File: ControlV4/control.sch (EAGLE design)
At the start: 45 parts, among them P1 CONNEC_1X03, P10 CONNEC_1X03, P11 CONNEC_1X03, P12 CONNEC_1X03, P2 CONNEC_1X03, P3 CONNEC_1X03, P4 CONNEC_1X03, P5 CONNEC_1X03, P6 CONNEC_1X03, P7 CONNEC_1X03, P8 CONNEC_1X03, P9 CONNEC_1X03

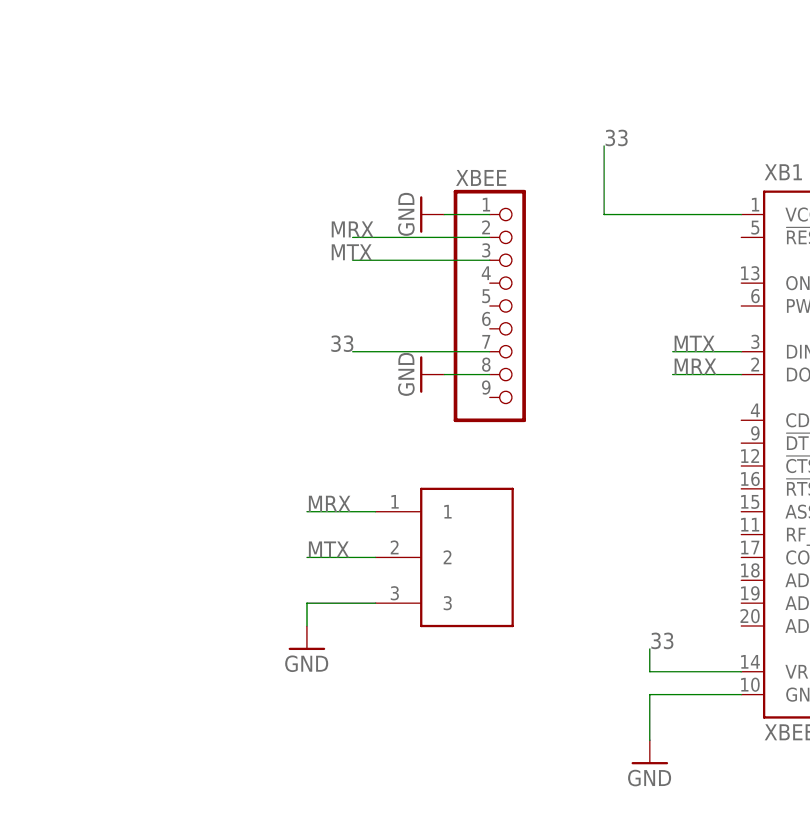
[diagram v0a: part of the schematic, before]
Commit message: Removing unused XBee port, changing extra serial port to 2.54
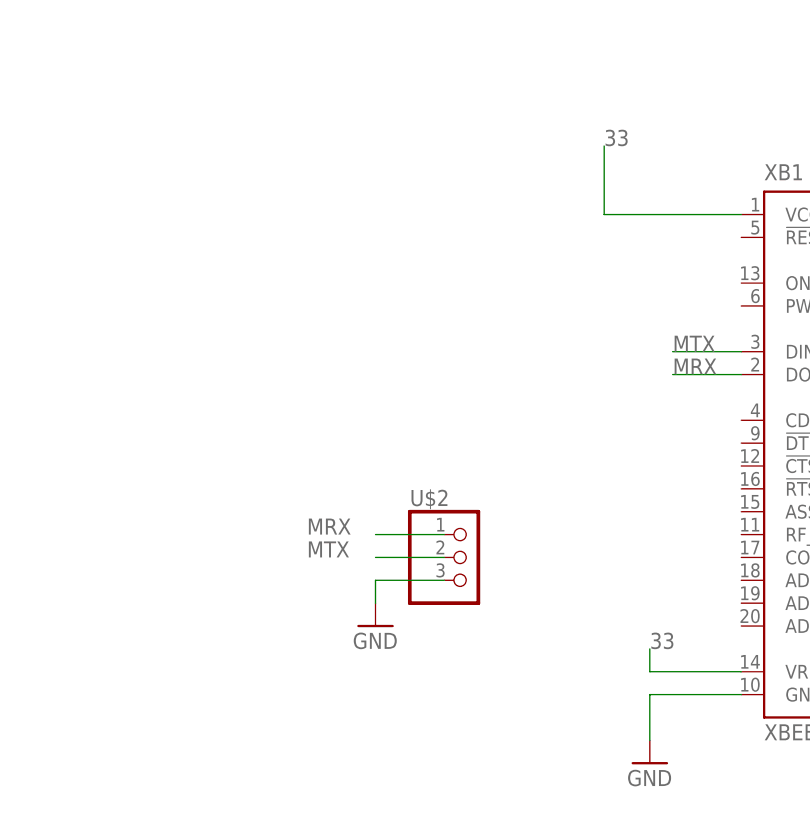
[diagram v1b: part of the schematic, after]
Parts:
- removed U$9: JST_3, perso:JST_3
- removed XBEE: CONNEC_1X09, rhoban:CONNEC_1X09
- added U$2: CONNEC_1X03, RobotCampus:CONNEC_1X03
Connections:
- net 33: no longer XBEE.7
- net GND: now also U$2.3; no longer U$9.3, XBEE.1, XBEE.8
- net MRX: now also U$2.1; no longer U$9.1, XBEE.2
- net MTX: now also U$2.2; no longer U$9.2, XBEE.3
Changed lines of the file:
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@@
 <part name="R11" library="rhoban" deviceset="RESISTANCE" device="-R0805"/>
 <part name="R12" library="rhoban" deviceset="RESISTANCE" device="-R0805"/>
-<part name="XBEE" library="rhoban" deviceset="CONNEC_1X09" device=""/>
-<part name="GND13" library="supply1" deviceset="GND" device=""/>
-<part name="GND14" library="supply1" deviceset="GND" device=""/>
 <part name="C1" library="rcl" deviceset="C-EU" device="075-032X103"/>
 <part name="C2" library="rcl" deviceset="C-EU" device="075-032X103"/>
@@
 <part name="GND15" library="supply1" deviceset="GND" device=""/>
 <part name="U$8" library="perso" deviceset="JST_2" device=""/>
-<part name="U$9" library="perso" deviceset="JST_3" device=""/>
 <part name="U$10" library="perso" deviceset="JST_2" device=""/>
 <part name="R13" library="rcl" deviceset="R-EU_" device="R0805"/>
@@
 <part name="U$12" library="RobotCampus" deviceset="DIODE" device=""/>
 <part name="JP1" library="pinhead" deviceset="PINHD-1X3" device=""/>
+<part name="U$2" library="RobotCampus" deviceset="CONNEC_1X03" device=""/>
 </parts>
 <sheets>
@@
 <instance part="P+2" gate="VCC" x="248.92" y="116.84"/>
 <instance part="GND3" gate="1" x="251.46" y="60.96"/>
-<instance part="GND4" gate="1" x="91.44" y="-22.86"/>
+<instance part="GND4" gate="1" x="99.06" y="-20.32"/>
 <instance part="GND5" gate="1" x="58.42" y="144.78"/>
 <instance part="P+3" gate="VCC" x="58.42" y="160.02"/>
@@
 <instance part="R11" gate="G$1" x="236.22" y="99.06"/>
 <instance part="R12" gate="G$1" x="236.22" y="106.68"/>
-<instance part="XBEE" gate="G$1" x="109.22" y="15.24"/>
-<instance part="GND13" gate="1" x="104.14" y="25.4" rot="R270"/>
-<instance part="GND14" gate="1" x="104.14" y="7.62" rot="R270"/>
 <instance part="C1" gate="G$1" x="210.82" y="152.4"/>
 <instance part="C2" gate="G$1" x="218.44" y="152.4"/>
@@
 <instance part="GND15" gate="1" x="58.42" y="127"/>
 <instance part="U$8" gate="G$1" x="73.66" y="132.08"/>
-<instance part="U$9" gate="G$1" x="109.22" y="-12.7"/>
 <instance part="U$10" gate="G$1" x="73.66" y="152.4"/>
 <instance part="R13" gate="G$1" x="45.72" y="91.44"/>
@@
 <instance part="U$12" gate="DIODE" x="157.48" y="172.72"/>
 <instance part="JP1" gate="A" x="187.96" y="170.18" rot="MR180"/>
+<instance part="U$2" gate="G$1" x="104.14" y="-15.24"/>
 </instances>
 <busses>
@@
 </segment>
 <segment>
-<pinref part="XBEE" gate="G$1" pin="1"/>
-<pinref part="GND13" gate="1" pin="GND"/>
-<wire x1="106.68" y1="25.4" x2="111.76" y2="25.4" width="0.1524" layer="91"/>
-</segment>
-<segment>
-<pinref part="XBEE" gate="G$1" pin="8"/>
-<pinref part="GND14" gate="1" pin="GND"/>
-<wire x1="106.68" y1="7.62" x2="111.76" y2="7.62" width="0.1524" layer="91"/>
-</segment>
-<segment>
 <pinref part="GND15" gate="1" pin="GND"/>
 <pinref part="U$8" gate="G$1" pin="GND"/>
 <wire x1="58.42" y1="129.54" x2="63.5" y2="129.54" width="0.1524" layer="91"/>
-</segment>
-<segment>
-<pinref part="U$9" gate="G$1" pin="3"/>
-<wire x1="99.06" y1="-17.78" x2="91.44" y2="-17.78" width="0.1524" layer="91"/>
-<wire x1="91.44" y1="-17.78" x2="91.44" y2="-20.32" width="0.1524" layer="91"/>
-<pinref part="GND4" gate="1" pin="GND"/>
 </segment>
 <segment>
@@
 <wire x1="129.54" y1="-27.94" x2="129.54" y2="-33.02" width="0.1524" layer="91"/>
 <pinref part="GND16" gate="1" pin="GND"/>
+</segment>
+<segment>
+<pinref part="U$2" gate="G$1" pin="3"/>
+<wire x1="106.68" y1="-15.24" x2="99.06" y2="-15.24" width="0.1524" layer="91"/>
+<pinref part="GND4" gate="1" pin="GND"/>
+<wire x1="99.06" y1="-15.24" x2="99.06" y2="-17.78" width="0.1524" layer="91"/>
 </segment>
 </net>
@@
 </segment>
 <segment>
-<pinref part="XBEE" gate="G$1" pin="3"/>
-<wire x1="111.76" y1="20.32" x2="96.52" y2="20.32" width="0.1524" layer="91"/>
-<label x="93.98" y="20.32" size="1.778" layer="95"/>
-</segment>
-<segment>
-<pinref part="U$9" gate="G$1" pin="2"/>
-<wire x1="99.06" y1="-12.7" x2="91.44" y2="-12.7" width="0.1524" layer="91"/>
-<label x="91.44" y="-12.7" size="1.778" layer="95"/>
-</segment>
-<segment>
 <pinref part="XB1" gate="G$1" pin="DIN/!CONFIG"/>
 <wire x1="139.7" y1="10.16" x2="132.08" y2="10.16" width="0.1524" layer="91"/>
 <label x="132.08" y="10.16" size="1.778" layer="95"/>
 </segment>
+<segment>
+<pinref part="U$2" gate="G$1" pin="2"/>
+<wire x1="106.68" y1="-12.7" x2="99.06" y2="-12.7" width="0.1524" layer="91"/>
+<label x="91.44" y="-12.7" size="1.778" layer="95"/>
+</segment>
 </net>
 <net name="MRX" class="0">
@@
 </segment>
 <segment>
-<pinref part="XBEE" gate="G$1" pin="2"/>
-<wire x1="111.76" y1="22.86" x2="96.52" y2="22.86" width="0.1524" layer="91"/>
-<label x="93.98" y="22.86" size="1.778" layer="95"/>
-</segment>
-<segment>
-<pinref part="U$9" gate="G$1" pin="1"/>
-<wire x1="99.06" y1="-7.62" x2="91.44" y2="-7.62" width="0.1524" layer="91"/>
-<label x="91.44" y="-7.62" size="1.778" layer="95"/>
-</segment>
-<segment>
 <pinref part="XB1" gate="G$1" pin="DOUT"/>
 <wire x1="139.7" y1="7.62" x2="132.08" y2="7.62" width="0.1524" layer="91"/>
 <label x="132.08" y="7.62" size="1.778" layer="95"/>
+</segment>
+<segment>
+<pinref part="U$2" gate="G$1" pin="1"/>
+<wire x1="106.68" y1="-10.16" x2="99.06" y2="-10.16" width="0.1524" layer="91"/>
+<label x="91.44" y="-10.16" size="1.778" layer="95"/>
 </segment>
 </net>
@@
 </segment>
 <segment>
-<pinref part="XBEE" gate="G$1" pin="7"/>
-<wire x1="111.76" y1="10.16" x2="96.52" y2="10.16" width="0.1524" layer="91"/>
-<label x="93.98" y="10.16" size="1.778" layer="95"/>
-</segment>
-<segment>

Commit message: Fixs
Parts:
- added C5: (no value), SparkFun-Capacitors:CAP_POLPTH2
- added R15, R16: (no value), rcl:R-EU_R0805
- added U$3: DIODE254, RobotCampus:DIODE254
- C3, C4: device rcl:C-EU075-032X103 -> SparkFun-Capacitors:CAP_POLPTH2
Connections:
- removed net MAPLE_VCC: C1.1, C2.1, JP1.2, R13.1, U$1.VIN, U$11.VIN
- removed net VCC: C3.1, C4.1, P1.2, P10.2, P11.2, P12.2, P2.2, P3.2, P4.2, P5.2, P6.2, P7.2, P8.2, P9.2, U$10.VCC
- new net N$13: R15.2, XB1.!RESET
- new net N$15: R16.2, XB1.ON/!SLEEP
- new net VMICRO: C3.+, C5.+, U$1.VIN, U$10.VCC, U$11.VIN, U$3.C
- new net VPOWER: C1.1, C2.1, C4.+, JP1.2, P1.2, P10.2, P11.2, P12.2, P2.2, P3.2, P4.2, P5.2, P6.2, P7.2, P8.2, P9.2, U$3.A
- net 33: now also R15.1, R16.1
- net GND: now also C3.-, C4.-, C5.-; no longer C3.2, C4.2
- net VCC_IN: now also R13.1

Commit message: Boarding
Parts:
- removed U$11: MCP1703SOT23-A, RobotCampus:MCP1703SOT23-A
- added C6: (no value), SparkFun-Capacitors:CAP_POLPTH2
- added U$4: MCP1703T-3302E/CB, RobotCampus:MCP1703T-3302E/CB
- renumbered U$10 to JST_MICRO, U$8 to JST_IN
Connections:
- new net 3.3: C6.+, U$4.VOUT
- net 33: no longer U$11.VOUT
- net GND: now also C6.-, U$4.GND; no longer U$11.GND
- net VMICRO: now also U$4.VIN; no longer U$11.VIN
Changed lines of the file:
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@@
 <part name="GPIO4" library="rhoban" deviceset="CONNEC_1X02" device=""/>
 <part name="GND6" library="supply1" deviceset="GND" device=""/>
-<part name="GND7" library="supply1" deviceset="GND" device=""/>
 <part name="GND8" library="supply1" deviceset="GND" device=""/>
 <part name="GND9" library="supply1" deviceset="GND" device=""/>
@@
 <part name="C2" library="rcl" deviceset="C-EU" device="075-032X103"/>
 <part name="GND15" library="supply1" deviceset="GND" device=""/>
-<part name="U$8" library="perso" deviceset="JST_2" device=""/>
-<part name="U$10" library="perso" deviceset="JST_2" device=""/>
+<part name="JST_IN" library="perso" deviceset="JST_2" device=""/>
+<part name="JST_MICRO" library="perso" deviceset="JST_2" device=""/>
 <part name="R13" library="rcl" deviceset="R-EU_" device="R0805"/>
 <part name="R14" library="rcl" deviceset="R-EU_" device="R0805"/>
@@
 <part name="XB1" library="maxstream" deviceset="XBEE" device="-PRO"/>
 <part name="GND16" library="supply1" deviceset="GND" device=""/>
-<part name="U$11" library="RobotCampus" deviceset="MCP1703" device="SOT23-A"/>
 <part name="U$12" library="RobotCampus" deviceset="DIODE" device=""/>
 <part name="JP1" library="pinhead" deviceset="PINHD-1X3" device=""/>
@@
 <part name="R15" library="rcl" deviceset="R-EU_" device="R0805"/>
 <part name="R16" library="rcl" deviceset="R-EU_" device="R0805"/>
+<part name="C6" library="SparkFun-Capacitors" deviceset="CAP_POL" device="PTH2"/>
+<part name="GND14" library="supply1" deviceset="GND" device=""/>
+<part name="U$4" library="RobotCampus" deviceset="MCP1703T-3302E/CB" device=""/>
+<part name="GND7" library="supply1" deviceset="GND" device=""/>
 </parts>
 <sheets>
@@
 <instance part="GPIO4" gate="G$1" x="251.46" y="-7.62" rot="R90"/>
 <instance part="GND6" gate="1" x="251.46" y="-12.7"/>
-<instance part="GND7" gate="1" x="160.02" y="119.38"/>
 <instance part="GND8" gate="1" x="218.44" y="142.24"/>
 <instance part="GND9" gate="1" x="210.82" y="142.24"/>
@@
 <instance part="C2" gate="G$1" x="218.44" y="152.4"/>
 <instance part="GND15" gate="1" x="58.42" y="127"/>
-<instance part="U$8" gate="G$1" x="73.66" y="132.08"/>
-<instance part="U$10" gate="G$1" x="73.66" y="152.4"/>
+<instance part="JST_IN" gate="G$1" x="73.66" y="132.08"/>
+<instance part="JST_MICRO" gate="G$1" x="73.66" y="152.4"/>
 <instance part="R13" gate="G$1" x="45.72" y="91.44"/>
 <instance part="R14" gate="G$1" x="53.34" y="86.36" rot="R90"/>
@@
 <instance part="XB1" gate="G$1" x="154.94" y="0"/>
 <instance part="GND16" gate="1" x="129.54" y="-35.56"/>
-<instance part="U$11" gate="G$1" x="160.02" y="152.4"/>
 <instance part="U$12" gate="DIODE" x="157.48" y="172.72"/>
 <instance part="JP1" gate="A" x="187.96" y="170.18" rot="MR180"/>
@@
 <instance part="R15" gate="G$1" x="134.62" y="22.86"/>
 <instance part="R16" gate="G$1" x="134.62" y="17.78"/>
+<instance part="C6" gate="G$1" x="276.86" y="152.4"/>
+<instance part="GND14" gate="1" x="276.86" y="142.24"/>
+<instance part="U$4" gate="A" x="149.86" y="149.86"/>
+<instance part="GND7" gate="1" x="129.54" y="139.7"/>
 </instances>
 <busses>
@@
 <pinref part="GND5" gate="1" pin="GND"/>
 <wire x1="58.42" y1="149.86" x2="58.42" y2="147.32" width="0.1524" layer="91"/>
-<pinref part="U$10" gate="G$1" pin="GND"/>
+<pinref part="JST_MICRO" gate="G$1" pin="GND"/>
 </segment>
 <segment>
@@
 </segment>
 <segment>
-<pinref part="GND7" gate="1" pin="GND"/>
-<wire x1="160.02" y1="121.92" x2="160.02" y2="142.24" width="0.1524" layer="91"/>
-<pinref part="U$11" gate="G$1" pin="GND"/>
-</segment>
-<segment>
 <pinref part="GND8" gate="1" pin="GND"/>
 <wire x1="218.44" y1="144.78" x2="218.44" y2="147.32" width="0.1524" layer="91"/>
@@
 <segment>
 <pinref part="GND15" gate="1" pin="GND"/>
-<pinref part="U$8" gate="G$1" pin="GND"/>
+<pinref part="JST_IN" gate="G$1" pin="GND"/>
 <wire x1="58.42" y1="129.54" x2="63.5" y2="129.54" width="0.1524" layer="91"/>
 </segment>
@@
 <pinref part="GND13" gate="1" pin="GND"/>
 <pinref part="C4" gate="G$1" pin="-"/>
+</segment>
+<segment>
+<pinref part="GND14" gate="1" pin="GND"/>
+<pinref part="C6" gate="G$1" pin="-"/>
+<wire x1="276.86" y1="144.78" x2="276.86" y2="147.32" width="0.1524" layer="91"/>
+</segment>
+<segment>
+<pinref part="U$4" gate="A" pin="GND"/>
+<pinref part="GND7" gate="1" pin="GND"/>
+<wire x1="132.08" y1="144.78" x2="129.54" y2="144.78" width="0.1524" layer="91"/>
+<wire x1="129.54" y1="144.78" x2="129.54" y2="142.24" width="0.1524" layer="91"/>
 </segment>
 </net>
@@
 </segment>
 </net>
-<net name="VPOWER" class="0">
+<net name="VPOWER" class="1">
 <segment>
 <wire x1="218.44" y1="154.94" x2="210.82" y2="154.94" width="0.1524" layer="91"/>
@@
 <net name="33" class="0">
 <segment>
-<wire x1="172.72" y1="154.94" x2="180.34" y2="154.94" width="0.1524" layer="91"/>
-<label x="180.34" y="154.94" size="1.778" layer="95"/>
-<pinref part="U$11" gate="G$1" pin="VOUT"/>
-</segment>
-<segment>
 <pinref part="XB1" gate="G$1" pin="VCC"/>
 <wire x1="139.7" y1="25.4" x2="124.46" y2="25.4" width="0.1524" layer="91"/>
@@
 <net name="VCC_IN" class="0">
 <segment>
-<pinref part="U$8" gate="G$1" pin="VCC"/>
+<pinref part="JST_IN" gate="G$1" pin="VCC"/>
 <wire x1="63.5" y1="134.62" x2="58.42" y2="134.62" width="0.1524" layer="91"/>
 <label x="50.8" y="134.62" size="1.778" layer="95"/>
@@
 <segment>
 <wire x1="63.5" y1="154.94" x2="58.42" y2="154.94" width="0.1524" layer="91"/>
-<pinref part="U$10" gate="G$1" pin="VCC"/>
+<pinref part="JST_MICRO" gate="G$1" pin="VCC"/>
 <label x="58.42" y="157.48" size="1.778" layer="95" rot="R180"/>
 </segment>
@@
 <wire x1="-33.02" y1="22.86" x2="-43.18" y2="22.86" width="0.1524" layer="91"/>
 <label x="-33.02" y="22.86" size="1.778" layer="95"/>
-</segment>
-<segment>
-<wire x1="147.32" y1="154.94" x2="139.7" y2="154.94" width="0.1524" layer="91"/>
-<label x="134.62" y="154.94" size="1.778" layer="95"/>
-<pinref part="U$11" gate="G$1" pin="VIN"/>
 </segment>
 <segment>
@@
 <junction x="243.84" y="154.94"/>
 </segment>
+<segment>
+<pinref part="U$4" gate="A" pin="VIN"/>
+<wire x1="132.08" y1="149.86" x2="127" y2="149.86" width="0.1524" layer="91"/>
+<label x="116.84" y="149.86" size="1.778" layer="95"/>
+</segment>
 </net>
 <net name="N$13" class="0">
@@
 </segment>
 </net>
+<net name="3.3" class="0">
+<segment>
+<pinref part="C6" gate="G$1" pin="+"/>
+<wire x1="276.86" y1="154.94" x2="276.86" y2="157.48" width="0.1524" layer="91"/>
+<label x="276.86" y="157.48" size="1.778" layer="95"/>
+</segment>
+<segment>
+<pinref part="U$4" gate="A" pin="VOUT"/>
+<wire x1="167.64" y1="149.86" x2="170.18" y2="149.86" width="0.1524" layer="91"/>
+<label x="170.18" y="149.86" size="1.778" layer="95"/>
+</segment>
+</net>

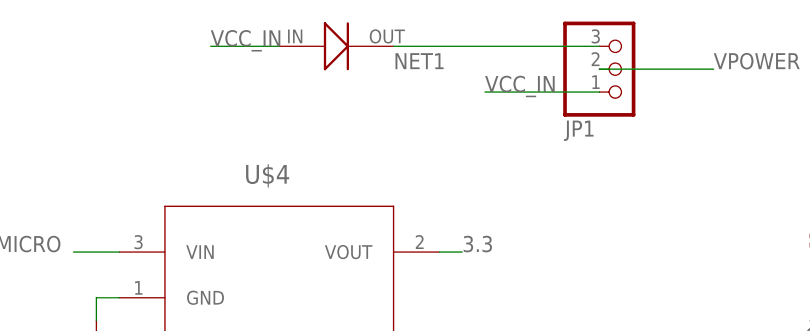
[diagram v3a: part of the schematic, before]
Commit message: Moving to official package for diode
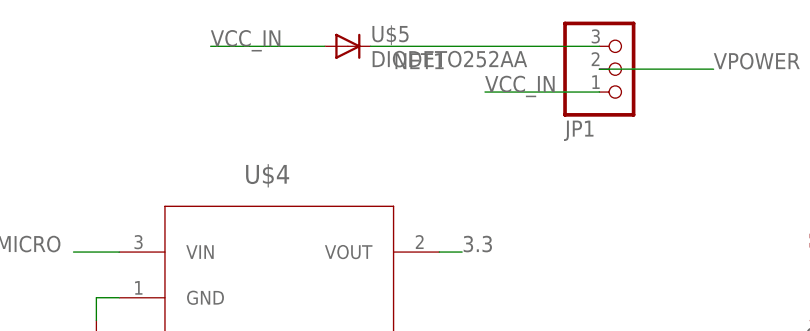
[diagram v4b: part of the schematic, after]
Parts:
- removed U$12: (no value), RobotCampus:DIODE
- added U$5: DIODETO252AA, RobotCampus:DIODETO252AA
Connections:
- net NET1: now also U$5.C; no longer U$12.OUT
- net VCC_IN: now also U$5.A; no longer U$12.IN
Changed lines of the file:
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@@
 <part name="XB1" library="maxstream" deviceset="XBEE" device="-PRO"/>
 <part name="GND16" library="supply1" deviceset="GND" device=""/>
-<part name="U$12" library="RobotCampus" deviceset="DIODE" device=""/>
 <part name="JP1" library="pinhead" deviceset="PINHD-1X3" device=""/>
 <part name="U$2" library="RobotCampus" deviceset="CONNEC_1X03" device=""/>
@@
 <part name="U$4" library="RobotCampus" deviceset="MCP1703T-3302E/CB" device=""/>
 <part name="GND7" library="supply1" deviceset="GND" device=""/>
+<part name="U$5" library="RobotCampus" deviceset="DIODE" device="TO252AA"/>
 </parts>
 <sheets>
@@
 <instance part="XB1" gate="G$1" x="154.94" y="0"/>
 <instance part="GND16" gate="1" x="129.54" y="-35.56"/>
-<instance part="U$12" gate="DIODE" x="157.48" y="172.72"/>
 <instance part="JP1" gate="A" x="187.96" y="170.18" rot="MR180"/>
 <instance part="U$2" gate="G$1" x="104.14" y="-15.24"/>
@@
 <instance part="U$4" gate="A" x="149.86" y="149.86"/>
 <instance part="GND7" gate="1" x="129.54" y="139.7"/>
+<instance part="U$5" gate="G$1" x="160.02" y="172.72"/>
 </instances>
 <busses>
@@
 </segment>
 <segment>
-<pinref part="U$12" gate="DIODE" pin="IN"/>
-<wire x1="149.86" y1="172.72" x2="142.24" y2="172.72" width="0.1524" layer="91"/>
+<wire x1="154.94" y1="172.72" x2="142.24" y2="172.72" width="0.1524" layer="91"/>
 <label x="142.24" y="172.72" size="1.778" layer="95"/>
+<pinref part="U$5" gate="G$1" pin="A"/>
 </segment>
 <segment>
@@
 <net name="NET1" class="0">
 <segment>
-<pinref part="U$12" gate="DIODE" pin="OUT"/>
 <label x="162.56" y="170.18" size="1.778" layer="95"/>
 <pinref part="JP1" gate="A" pin="3"/>
-<wire x1="162.56" y1="172.72" x2="185.42" y2="172.72" width="0.1524" layer="91"/>
-</segment>
-</net>
+<wire x1="160.02" y1="172.72" x2="185.42" y2="172.72" width="0.1524" layer="91"/>
+<pinref part="U$5" gate="G$1" pin="C"/>
+</segment>
+</net>
